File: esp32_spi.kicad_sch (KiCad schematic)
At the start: 21 parts, among them U201 SN74LV1T34, U202 SN74LV1T34, U203 74AHCT595, U204 SN74LV1T34, U205 74AHCT595, U206 ESP32-WROOM-32, U207 74AHCT595

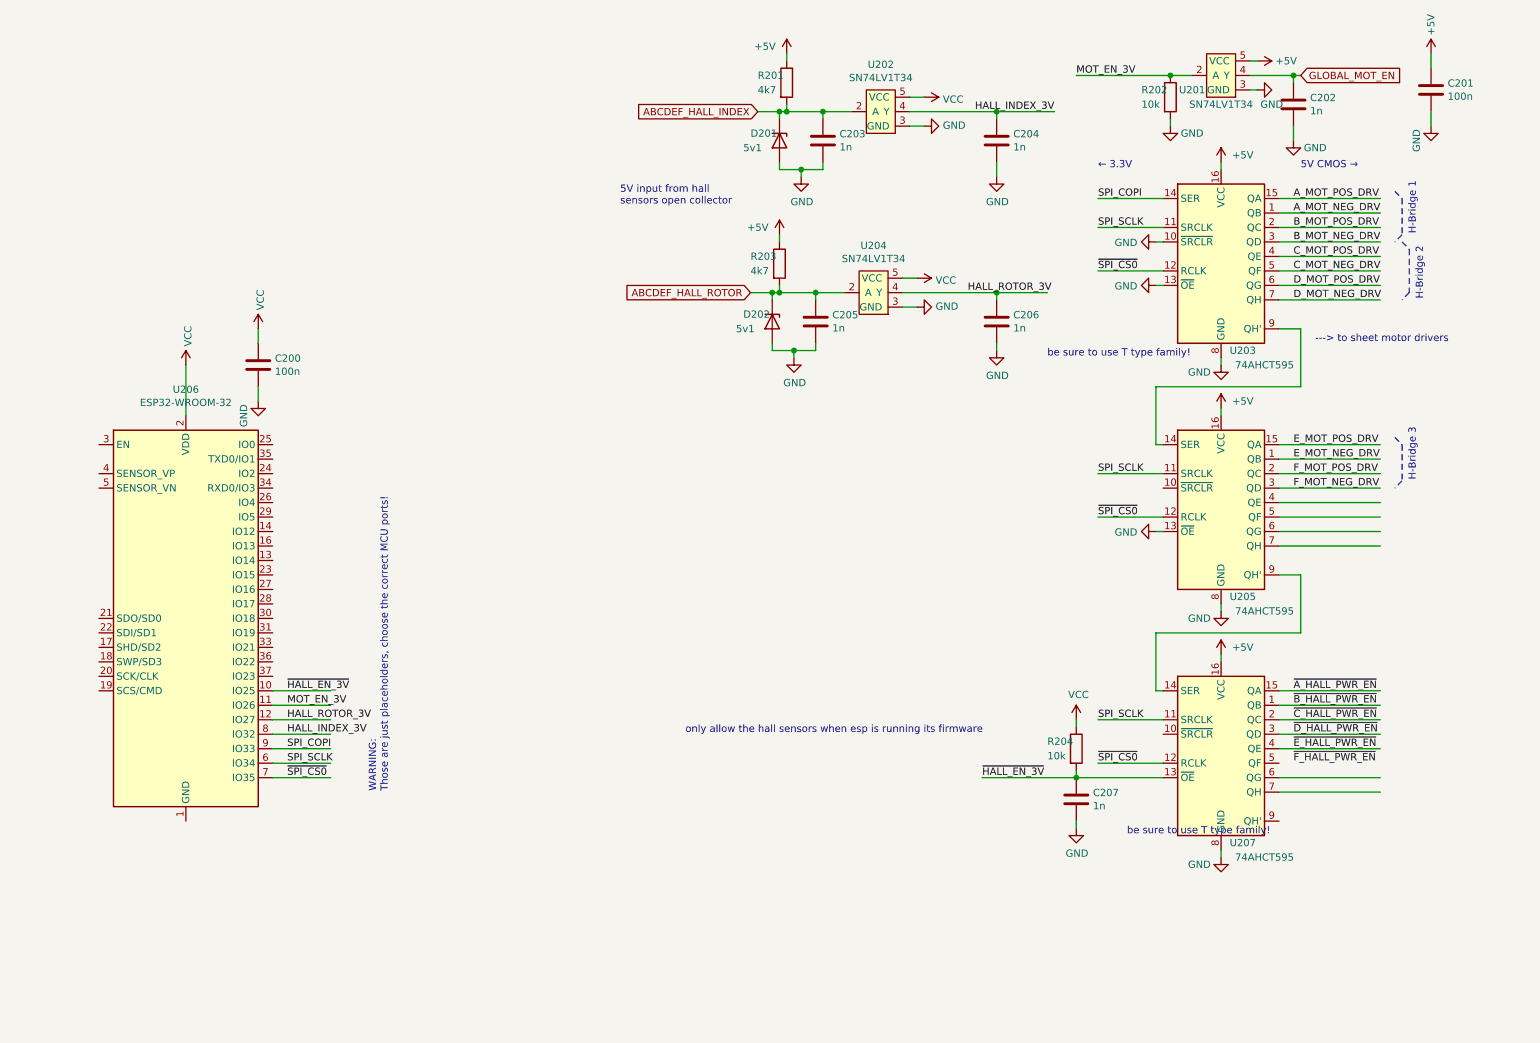
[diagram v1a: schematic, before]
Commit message: more C vor Logic and placing first groups of parts
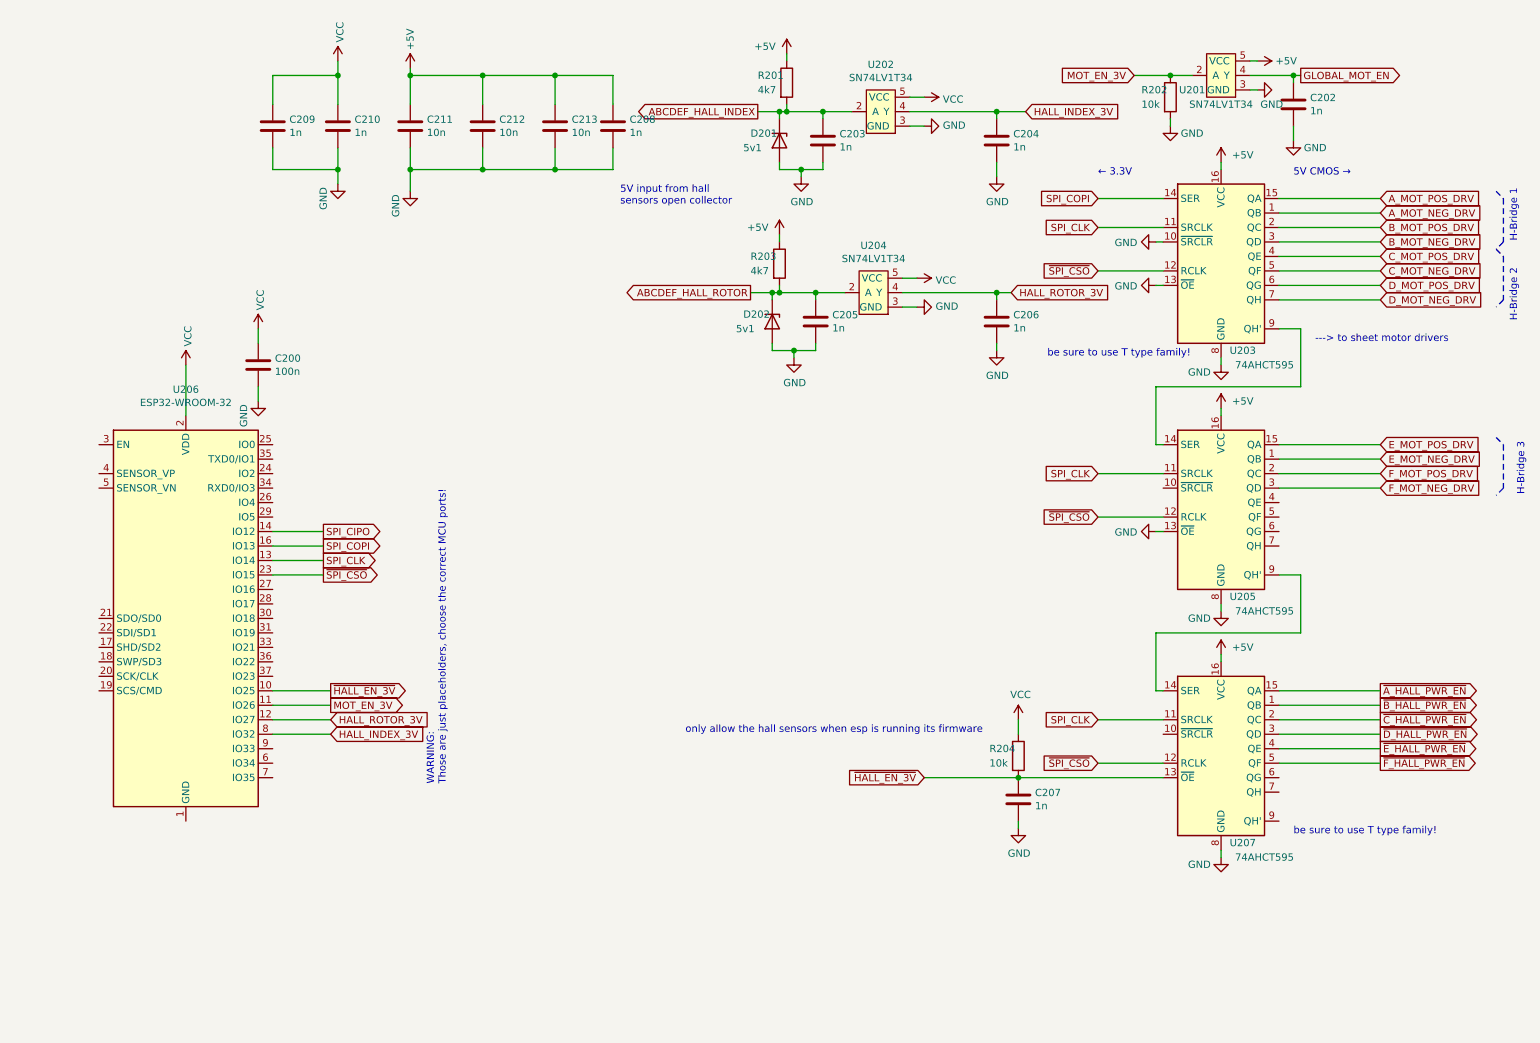
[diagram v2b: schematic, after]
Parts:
- removed C201: 100n, Capacitor_SMD:C_0603_1608Metric, symbol Device:C
- added C208, C209, C210: 1n, Capacitor_SMD:C_0603_1608Metric, symbol Device:C
- added C211, C212, C213: 10n, Capacitor_SMD:C_0603_1608Metric, symbol Device:C
- D201, D202: footprint Diode_SMD:D_SMB_Handsoldering -> Diode_SMD:D_SOT-23_ANK; Link https://www.reichelt.de/zenerdiode-5-1-v-3-w-smb-1smb-5918b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 -> https://www.reichelt.de/zenerdiode-5-1-v-0-35-w-sot-23-smd-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
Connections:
- net +5V: now also C208.1, C211.1, C212.1, C213.1
- net GND: now also C208.2, C209.2, C210.2, C211.2, C212.2, C213.2
- net SPI_COPI: now also U206.16 (IO13); no longer U206.9 (IO33)
- net VCC: now also C209.1, C210.1
- net ~F_HALL_PWR_EN~: now also U207.5 (QF)
- net SPI_CLK: now reaches U206.13 (IO14)
- net SPI_CLK: now also U203.11 (SRCLK), U205.11 (SRCLK), U207.11 (SRCLK)
- net SPI_CIPO: now reaches U206.14 (IO12)
- net ~SPI_CSO~: now reaches U206.23 (IO15)
- net ~SPI_CSO~: now also U203.12 (RCLK), U205.12 (RCLK), U207.12 (RCLK)
- removed net SPI_SCLK: U203.11 (SRCLK), U205.11 (SRCLK), U206.6 (IO34), U207.11 (SRCLK)
- removed net ~SPI_CS0~: U203.12 (RCLK), U205.12 (RCLK), U206.7 (IO35), U207.12 (RCLK)
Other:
- moved on the sheet: C207, R204

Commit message: esp32-spi: changed labels, C removed, esp32 programming
* Added esp32 programming connector + buttons for reset, gpio0
* Removed C on local signals (between to chips on board)
    (3.3v between ESP and voltage translators)
* changed some labels from globals to local labels on sheet
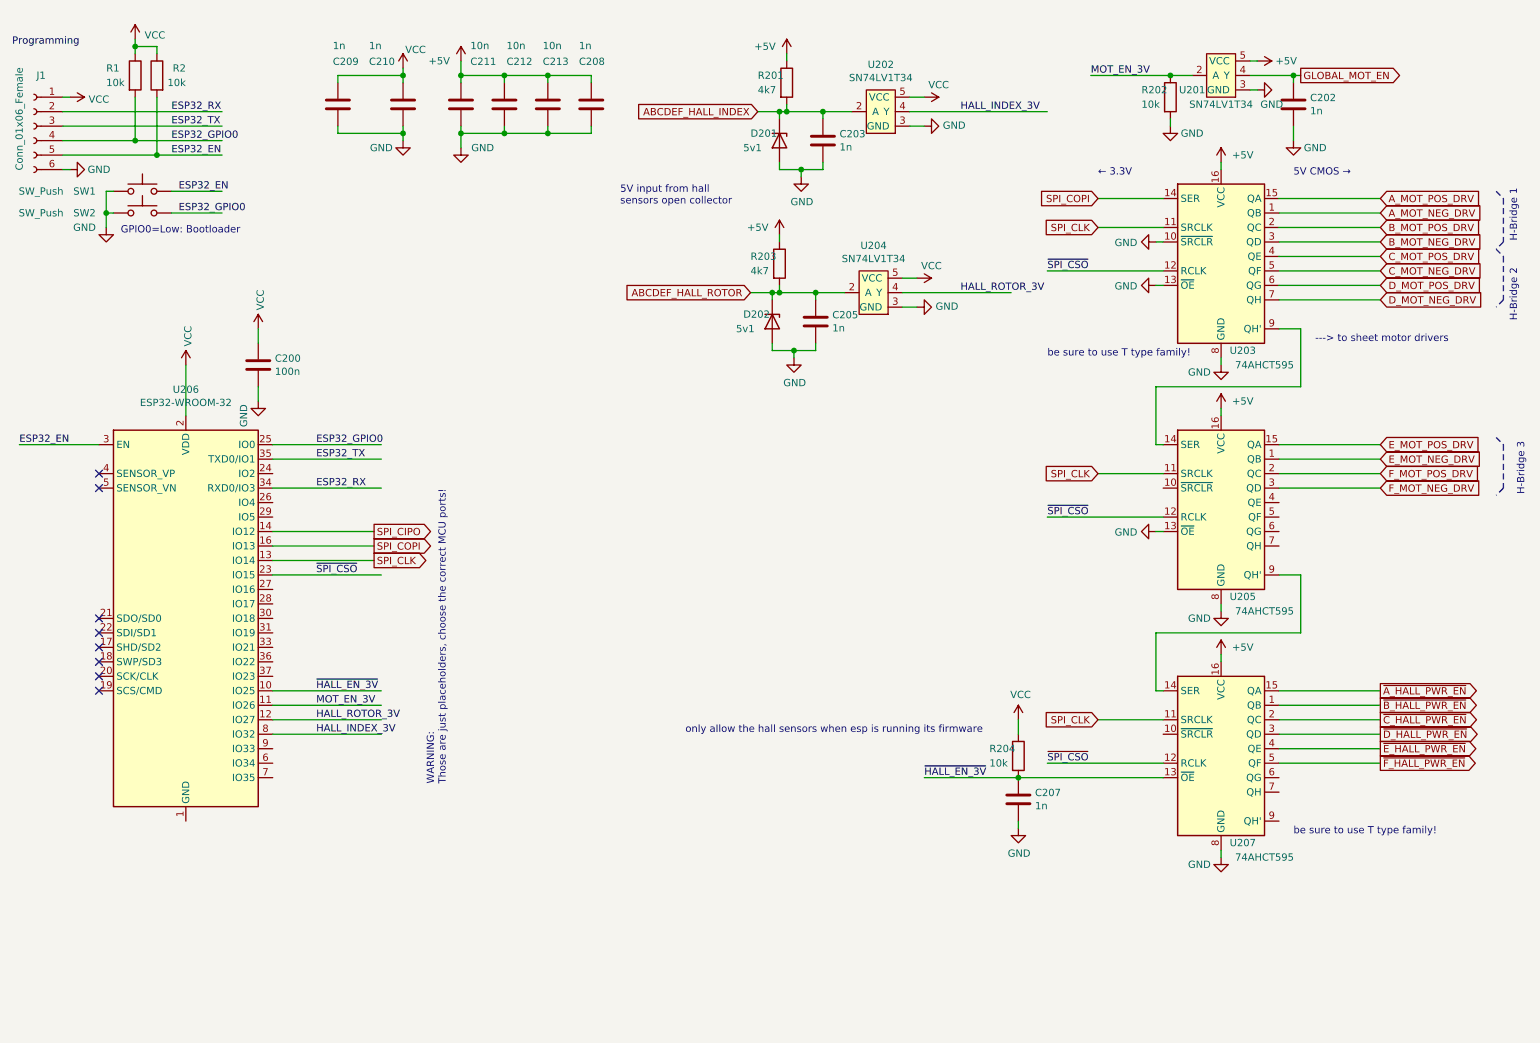
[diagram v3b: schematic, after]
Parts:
- removed C204, C206: 1n, Capacitor_SMD:C_0603_1608Metric, symbol Device:C
- added J1: Conn_01x06_Female, symbol Connector:Conn_01x06_Female
- added R1, R2: 10k, Resistor_SMD:R_0603_1608Metric, symbol Device:R
- added SW1, SW2: SW_Push, symbol Switch:SW_Push
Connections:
- net GND: now also J1.6 (Pin_6), SW1.1, SW2.1
- net VCC: now also J1.1 (Pin_1), R1.1, R2.1
- net ESP32_GPIO0: now reaches U206.25 (IO0)
- net ESP32_GPIO0: now also J1.4 (Pin_4), R1.2, SW2.2
- net ESP32_EN: now reaches U206.3 (EN)
- net ESP32_EN: now also J1.5 (Pin_5), R2.2, SW1.2
- net ESP32_RX: now reaches U206.34 (RXD0/IO3)
- net ESP32_RX: now also J1.2 (Pin_2)
- net ESP32_TX: now reaches U206.35 (TXD0/IO1)
- net ESP32_TX: now also J1.3 (Pin_3)
- no-connect marks 0 -> 8
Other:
- note added: "GPIO0=Low: Bootloader"
- moved on the sheet: C208, C209, C210, C211, C212, C213

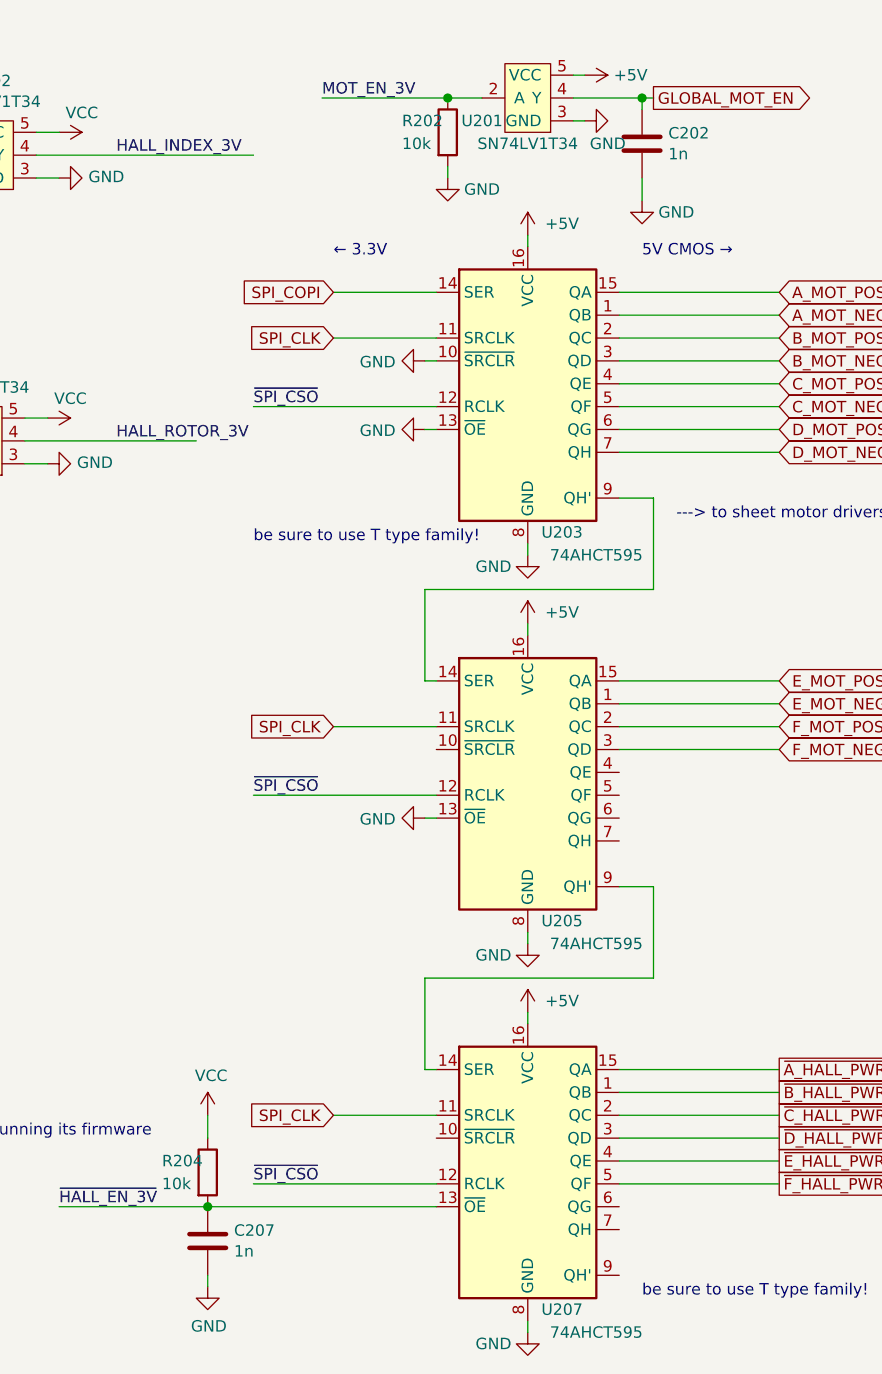
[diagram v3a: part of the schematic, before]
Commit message: Removing a few more unnecessary 1nF.
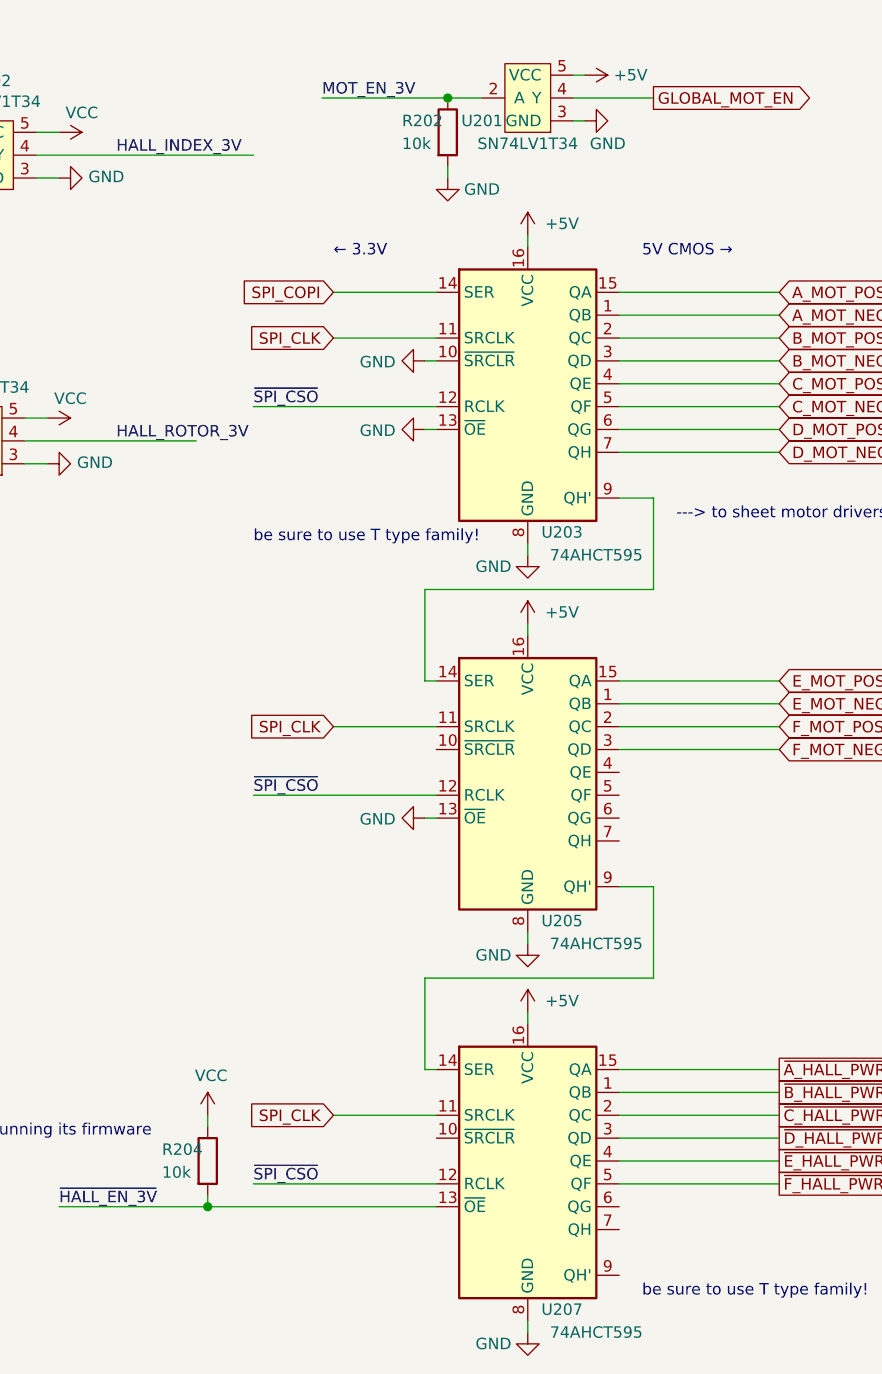
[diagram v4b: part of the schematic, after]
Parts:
- removed C202, C207: 1n, Capacitor_SMD:C_0603_1608Metric, symbol Device:C
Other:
- moved on the sheet: R204

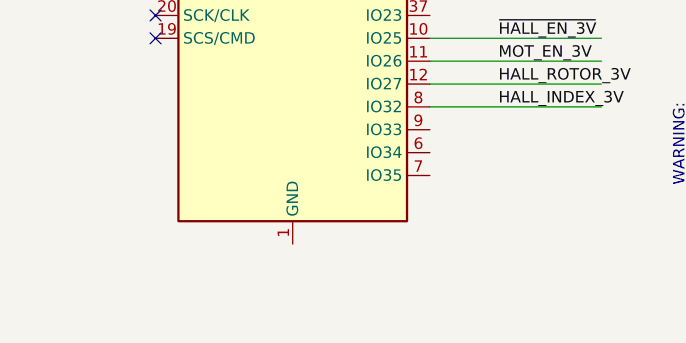
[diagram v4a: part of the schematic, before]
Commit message: all traces routed. ready for cleanup
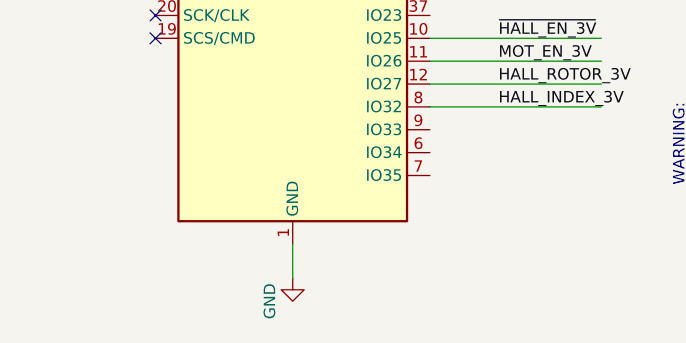
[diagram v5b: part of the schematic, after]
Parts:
- J1: footprint (none) -> Connector_PinHeader_2.54mm:PinHeader_1x06_P2.54mm_Vertical; Distri (none) -> Reichelt; Link (none) -> https://www.reichelt.de/smd-kurzhubtaster-vert-montage-hoeh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
- SW1, SW2: footprint (none) -> autophon-nerdblatt:NAMAE_JTP-1138
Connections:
- net GND: now also U206.1 (GND), U206.15 (GND), U206.38 (GND), U206.39 (GND)
